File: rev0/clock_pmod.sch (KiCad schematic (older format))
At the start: 3 parts, among them IC1 ECP5-BGA256

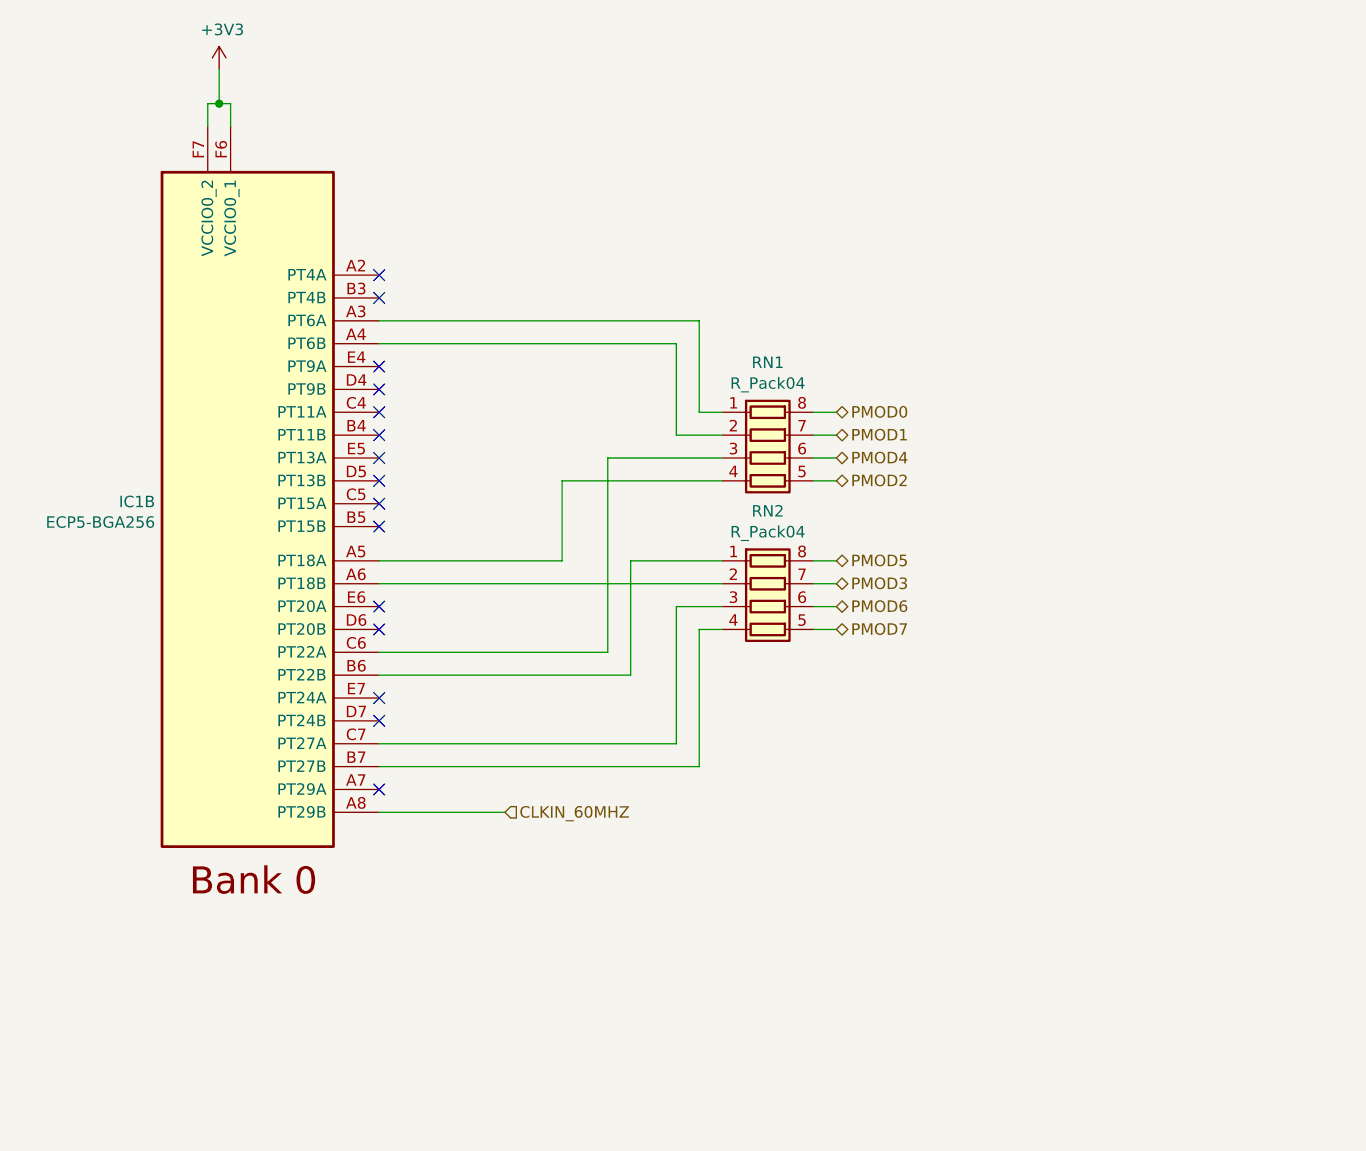
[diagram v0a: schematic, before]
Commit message: hardware: rearrange schematic for clarity
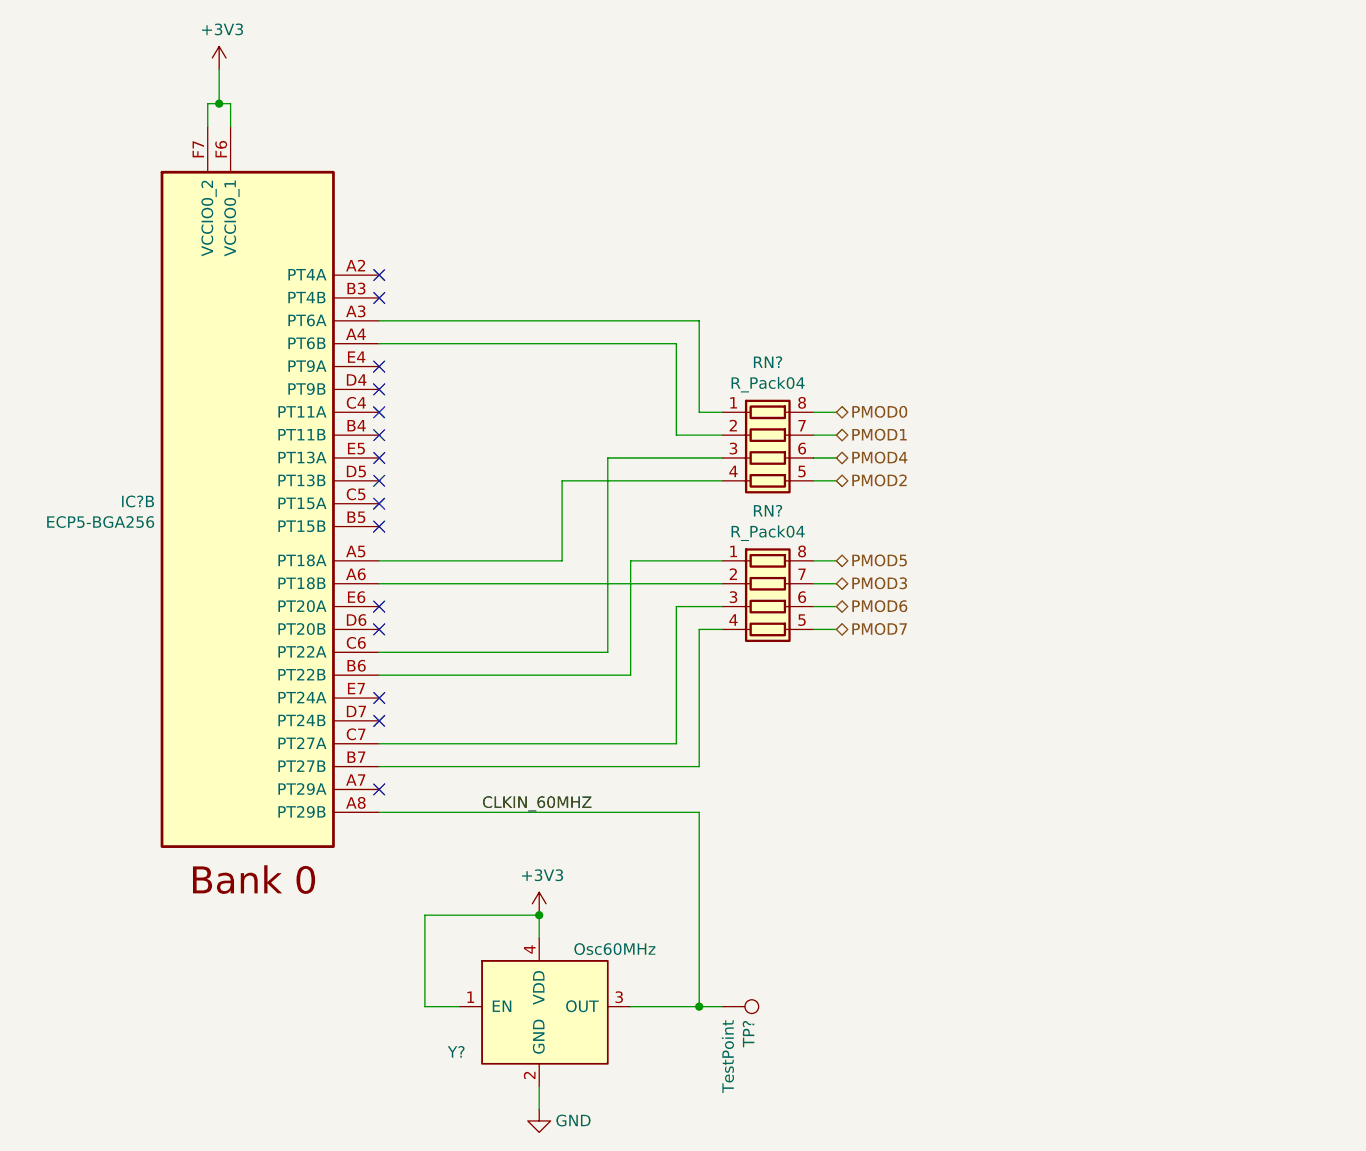
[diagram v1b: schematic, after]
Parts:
- added TP1: TestPoint, TestPoint:TestPoint_Pad_D1.0mm, symbol Connector:TestPoint
- added Y1: Osc60MHz, Crystal:Crystal_SMD_3225-4Pin_3.2x2.5mm, symbol support_hardware:DSC60xx
- renumbered IC1 to IC?
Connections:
- net +3V3: now also Y1.1 (EN), Y1.4 (VDD)
- net CLKIN_60MHZ: now also TP1.1, Y1.3 (OUT)
- new net GND: Y1.2 (GND)
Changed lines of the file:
@@
 encoding utf-8
 Sheet 9 9
-Title "LUNA: Debug and Control Connections"
-Date "2020-12-23"
+Title "LUNA: Clock and PMOD"
+Date "2020-12-24"
 Rev "r0"
 Comp "Great Scott Gadgets"
@@
 Wire Wire Line
 	2450 1650 2500 1650
-Text HLabel 3700 4750 2    50   Input ~ 0
-CLKIN_60MHZ
 NoConn ~ 3150 2500
 NoConn ~ 3150 2800
@@
 NoConn ~ 3150 4350
 $Comp
-L power:+3V3 #PWR0105
+L power:+3V3 #PWR?
 U 1 1 5E3ECE52
 P 2450 1500
-F 0 "#PWR0105" H 2450 1350 50  0001 C CNN
+F 0 "#PWR?" H 2450 1350 50  0001 C CNN
 F 1 "+3V3" H 2464 1673 50  0000 C CNN
 F 2 "" H 2450 1500 50  0001 C CNN
@@
 $EndComp
 Wire Wire Line
-	3150 4750 3700 4750
+	3150 4750 4550 4750
 $Comp
 L Device:R_Pack04 RN?
@@
 AR Path="/61658D8E" Ref="RN?"  Part="1"
 AR Path="/5DF88884/61658D8E" Ref="RN1"  Part="1"
-F 0 "RN1" V 4433 3200 50  0000 C CNN
+F 0 "RN?" V 4433 3200 50  0000 C CNN
 F 1 "R_Pack04" V 4524 3200 50  0000 C CNN
 F 2 "Resistor_SMD:R_Array_Convex_4x0402" V 5125 3200 50  0001 C CNN
@@
 AR Path="/61658D97" Ref="RN?"  Part="1"
 AR Path="/5DF88884/61658D97" Ref="RN2"  Part="1"
-F 0 "RN2" V 4433 3850 50  0000 C CNN
+F 0 "RN?" V 4433 3850 50  0000 C CNN
 F 1 "R_Pack04" V 4524 3850 50  0000 C CNN
 F 2 "Resistor_SMD:R_Array_Convex_4x0402" V 5125 3850 50  0001 C CNN
@@
 NoConn ~ 3150 4650
 $Comp
-L fpgas_and_processors:ECP5-BGA256 IC1
+L fpgas_and_processors:ECP5-BGA256 IC?
 U 2 1 5DFF5299
 P 2200 1950
-F 0 "IC1" H 2170 508 50  0000 R CNN
+F 0 "IC?" H 2170 508 50  0000 R CNN
 F 1 "ECP5-BGA256" H 2170 418 50  0000 R CNN
 F 2 "luna:lattice_cabga256" H -1000 5400 50  0001 L CNN
@@
 Wire Wire Line
 	4450 4450 3150 4450
+$Comp
+L support_hardware:DSC60xx Y?
+U 1 1 604A6A9B
+P 3600 5400
+AR Path="/604A6A9B" Ref="Y?"  Part="1"
+AR Path="/5DF88884/604A6A9B" Ref="Y1"  Part="1"
+F 0 "Y?" H 3450 5000 50  0000 L CNN
+F 1 "Osc60MHz" H 4000 5450 50  0000 L CNN
+F 2 "Crystal:Crystal_SMD_3225-4Pin_3.2x2.5mm" H 3600 5400 50  0001 C CNN
+F 3 "" H 3600 5400 50  0001 C CNN
+F 4 "MEMS OSC XO 60.0000MHZ H/LV-CMOS" H 3600 5400 50  0001 C CNN "Description"
+F 5 "SiTIME" H 3600 5400 50  0001 C CNN "Manufacturer"
+F 6 "SIT1602BC-23-33E-60.000000E" H 3600 5400 50  0001 C CNN "Part Number"
+	1    3600 5400
+	1    0    0    -1
+$EndComp
+Wire Wire Line
+	3500 5600 3350 5600
+Wire Wire Line
+	3350 5600 3350 5200
+Wire Wire Line
+	3850 5200 3850 5300
+$Comp
+L power:+3V3 #PWR?
+U 1 1 604A6AA4
+P 3850 5200
+AR Path="/604A6AA4" Ref="#PWR?"  Part="1"
+AR Path="/5DF88884/604A6AA4" Ref="#PWR011"  Part="1"
+F 0 "#PWR?" H 3850 5050 50  0001 C CNN
+F 1 "+3V3" H 3864 5373 50  0000 C CNN
+F 2 "" H 3850 5200 50  0001 C CNN
+F 3 "" H 3850 5200 50  0001 C CNN
+	1    3850 5200
+	1    0    0    -1
+$EndComp
+$Comp
+L power:GND #PWR?
+U 1 1 604A6AAA
+P 3850 6050
+AR Path="/604A6AAA" Ref="#PWR?"  Part="1"
+AR Path="/5DF88884/604A6AAA" Ref="#PWR018"  Part="1"
+F 0 "#PWR?" H 3850 5800 50  0001 C CNN
+F 1 "GND" H 4000 6000 50  0000 C CNN
+F 2 "" H 3850 6050 50  0001 C CNN
+F 3 "" H 3850 6050 50  0001 C CNN
+	1    3850 6050
+	1    0    0    -1
+$EndComp
+Wire Wire Line
+	3850 6050 3850 5950
+Wire Wire Line
+	3350 5200 3850 5200
+Connection ~ 3850 5200
+$Comp
+L Connector:TestPoint TP?
+U 1 1 604A6AB4
+P 4650 5600
+AR Path="/604A6AB4" Ref="TP?"  Part="1"
+AR Path="/5DF88884/604A6AB4" Ref="TP1"  Part="1"
+F 0 "TP?" H 4708 5718 50  0000 L CNN
+F 1 "TestPoint" H 4708 5628 50  0000 L CNN
+F 2 "TestPoint:TestPoint_Pad_D1.0mm" H 4850 5600 50  0001 C CNN
+F 3 "~" H 4850 5600 50  0001 C CNN
+F 4 "DNP" H 4650 5600 50  0001 C CNN "Note"
+	1    4650 5600
+	0    1    1    0
+$EndComp
+Wire Wire Line
+	4250 5600 4550 5600
+Wire Wire Line
+	4550 4750 4550 5600
+Connection ~ 4550 5600
+Wire Wire Line
+	4550 5600 4650 5600
+Text Label 3600 4750 0    50   ~ 0
+CLKIN_60MHZ
 $EndSCHEMATC

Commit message: hardware: clear up ERC errors
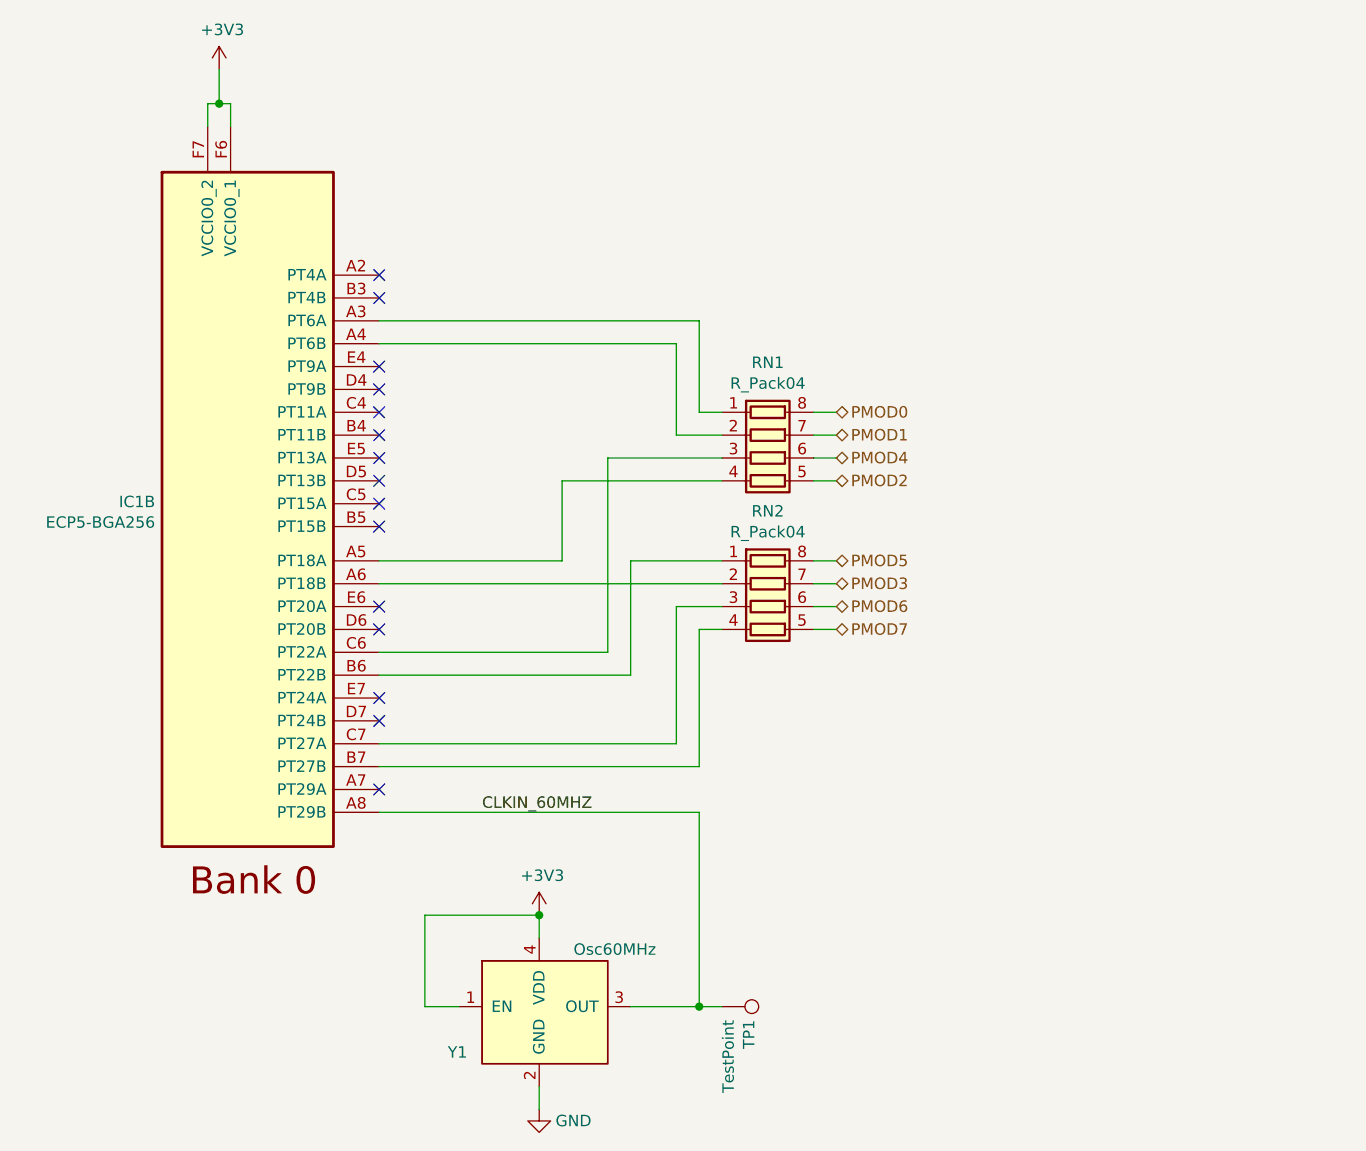
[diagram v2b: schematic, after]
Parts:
- gave numbers to parts that had none: 1
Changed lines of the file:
@@
 NoConn ~ 3150 4350
 $Comp
-L power:+3V3 #PWR?
+L power:+3V3 #PWR0105
 U 1 1 5E3ECE52
 P 2450 1500
-F 0 "#PWR?" H 2450 1350 50  0001 C CNN
+F 0 "#PWR0105" H 2450 1350 50  0001 C CNN
 F 1 "+3V3" H 2464 1673 50  0000 C CNN
 F 2 "" H 2450 1500 50  0001 C CNN
@@
 AR Path="/61658D8E" Ref="RN?"  Part="1"
 AR Path="/5DF88884/61658D8E" Ref="RN1"  Part="1"
-F 0 "RN?" V 4433 3200 50  0000 C CNN
+F 0 "RN1" V 4433 3200 50  0000 C CNN
 F 1 "R_Pack04" V 4524 3200 50  0000 C CNN
 F 2 "Resistor_SMD:R_Array_Convex_4x0402" V 5125 3200 50  0001 C CNN
@@
 AR Path="/61658D97" Ref="RN?"  Part="1"
 AR Path="/5DF88884/61658D97" Ref="RN2"  Part="1"
-F 0 "RN?" V 4433 3850 50  0000 C CNN
+F 0 "RN2" V 4433 3850 50  0000 C CNN
 F 1 "R_Pack04" V 4524 3850 50  0000 C CNN
 F 2 "Resistor_SMD:R_Array_Convex_4x0402" V 5125 3850 50  0001 C CNN
@@
 NoConn ~ 3150 4650
 $Comp
-L fpgas_and_processors:ECP5-BGA256 IC?
+L fpgas_and_processors:ECP5-BGA256 IC1
 U 2 1 5DFF5299
 P 2200 1950
-F 0 "IC?" H 2170 508 50  0000 R CNN
+F 0 "IC1" H 2170 508 50  0000 R CNN
 F 1 "ECP5-BGA256" H 2170 418 50  0000 R CNN
 F 2 "luna:lattice_cabga256" H -1000 5400 50  0001 L CNN
@@
 AR Path="/604A6A9B" Ref="Y?"  Part="1"
 AR Path="/5DF88884/604A6A9B" Ref="Y1"  Part="1"
-F 0 "Y?" H 3450 5000 50  0000 L CNN
+F 0 "Y1" H 3450 5000 50  0000 L CNN
 F 1 "Osc60MHz" H 4000 5450 50  0000 L CNN
 F 2 "Crystal:Crystal_SMD_3225-4Pin_3.2x2.5mm" H 3600 5400 50  0001 C CNN
@@
 AR Path="/604A6AA4" Ref="#PWR?"  Part="1"
 AR Path="/5DF88884/604A6AA4" Ref="#PWR011"  Part="1"
-F 0 "#PWR?" H 3850 5050 50  0001 C CNN
+F 0 "#PWR011" H 3850 5050 50  0001 C CNN
 F 1 "+3V3" H 3864 5373 50  0000 C CNN
 F 2 "" H 3850 5200 50  0001 C CNN
@@
 AR Path="/604A6AAA" Ref="#PWR?"  Part="1"
 AR Path="/5DF88884/604A6AAA" Ref="#PWR018"  Part="1"
-F 0 "#PWR?" H 3850 5800 50  0001 C CNN
+F 0 "#PWR018" H 3850 5800 50  0001 C CNN
 F 1 "GND" H 4000 6000 50  0000 C CNN
 F 2 "" H 3850 6050 50  0001 C CNN
@@
 AR Path="/604A6AB4" Ref="TP?"  Part="1"
 AR Path="/5DF88884/604A6AB4" Ref="TP1"  Part="1"
-F 0 "TP?" H 4708 5718 50  0000 L CNN
+F 0 "TP1" H 4708 5718 50  0000 L CNN
 F 1 "TestPoint" H 4708 5628 50  0000 L CNN
 F 2 "TestPoint:TestPoint_Pad_D1.0mm" H 4850 5600 50  0001 C CNN

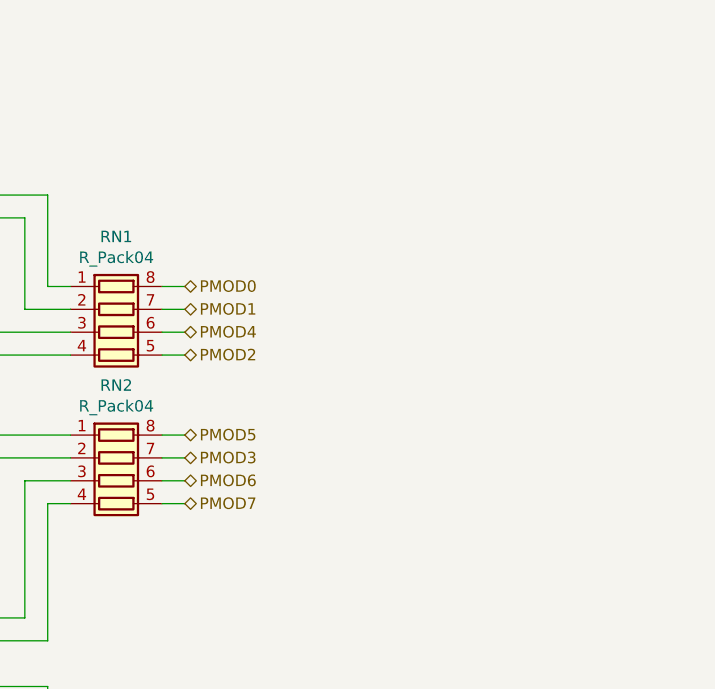
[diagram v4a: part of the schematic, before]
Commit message: hardware: add second PMOD connector (J11)
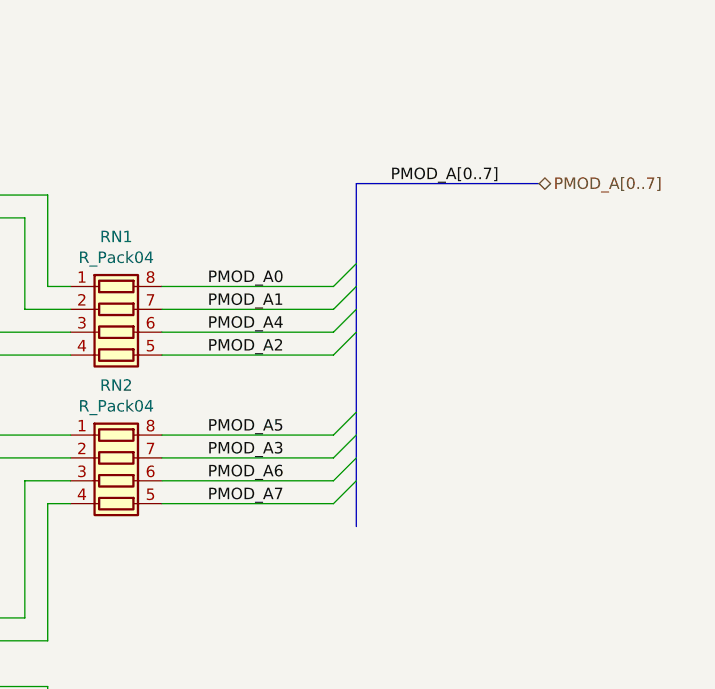
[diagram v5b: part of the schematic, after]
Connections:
- net PMOD0 renamed PMOD_A0
- net PMOD1 renamed PMOD_A1
- net PMOD2 renamed PMOD_A2
- net PMOD3 renamed PMOD_A3
- net PMOD4 renamed PMOD_A4
- net PMOD5 renamed PMOD_A5
- net PMOD6 renamed PMOD_A6
- net PMOD7 renamed PMOD_A7
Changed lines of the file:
@@
 Sheet 9 9
 Title "LUNA: Clock and PMOD"
-Date "2020-12-31"
+Date "2021-01-03"
 Rev "r0"
 Comp "Great Scott Gadgets"
@@
 	0    1    1    0
 $EndComp
-Text HLabel 5150 3850 2    50   BiDi ~ 0
-PMOD6
-Text HLabel 5150 3950 2    50   BiDi ~ 0
-PMOD7
-Text HLabel 5150 3000 2    50   BiDi ~ 0
-PMOD0
-Text HLabel 5150 3100 2    50   BiDi ~ 0
-PMOD1
-Text HLabel 5150 3300 2    50   BiDi ~ 0
-PMOD2
-Text HLabel 5150 3750 2    50   BiDi ~ 0
-PMOD3
-Text HLabel 5150 3200 2    50   BiDi ~ 0
-PMOD4
-Text HLabel 5150 3650 2    50   BiDi ~ 0
-PMOD5
 Wire Wire Line
 	4550 3000 4650 3000
@@
 NoConn ~ 3150 2400
 Wire Wire Line
-	5050 3950 5150 3950
-Wire Wire Line
-	5050 3850 5150 3850
-Wire Wire Line
-	5050 3750 5150 3750
-Wire Wire Line
-	5050 3650 5150 3650
-Wire Wire Line
-	5050 3300 5150 3300
-Wire Wire Line
-	5050 3200 5150 3200
-Wire Wire Line
-	5050 3100 5150 3100
-Wire Wire Line
-	5050 3000 5150 3000
+	5050 3950 5800 3950
+Wire Wire Line
+	5050 3850 5800 3850
+Wire Wire Line
+	5050 3750 5800 3750
+Wire Wire Line
+	5050 3650 5800 3650
+Wire Wire Line
+	5050 3300 5800 3300
+Wire Wire Line
+	5050 3200 5800 3200
+Wire Wire Line
+	5050 3100 5800 3100
+Wire Wire Line
+	5050 3000 5800 3000
 NoConn ~ 3150 4650
 $Comp
@@
 Text Label 3600 4750 0    50   ~ 0
 CLKIN_60MHZ
+Text Label 5250 3000 0    50   ~ 0
+PMOD_A0
+Text Label 5250 3100 0    50   ~ 0
+PMOD_A1
+Text Label 5250 3200 0    50   ~ 0
+PMOD_A4
+Text Label 5250 3300 0    50   ~ 0
+PMOD_A2
+Text Label 5250 3650 0    50   ~ 0
+PMOD_A5
+Text Label 5250 3750 0    50   ~ 0
+PMOD_A3
+Text Label 5250 3850 0    50   ~ 0
+PMOD_A6
+Text Label 5250 3950 0    50   ~ 0
+PMOD_A7
+Wire Bus Line
+	5900 2550 6700 2550
+Text Label 6050 2550 0    50   ~ 0
+PMOD_A[0..7]
+Text HLabel 6700 2550 2    50   BiDi ~ 0
+PMOD_A[0..7]
+Entry Wire Line
+	5800 3000 5900 2900
+Entry Wire Line
+	5800 3100 5900 3000
+Entry Wire Line
+	5800 3200 5900 3100
+Entry Wire Line
+	5800 3300 5900 3200
+Entry Wire Line
+	5800 3650 5900 3550
+Entry Wire Line
+	5800 3750 5900 3650
+Entry Wire Line
+	5800 3850 5900 3750
+Entry Wire Line
+	5800 3950 5900 3850
+Wire Bus Line
+	5900 2550 5900 4050
 $EndSCHEMATC
